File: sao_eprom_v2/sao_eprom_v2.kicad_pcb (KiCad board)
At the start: 4 copper layers, 65.1 x 55.1 mm, 75 parts, among them J1 Conn_01x03, J2 USB_C_Receptacle_USB2.0, J3 sao_v2_addon_tht, Q1 RE1C002UNTCL, Q2 RE1C002ZPTL, Q3 RE1C002UNTCL, Q4 RE1C002ZPTL, Q5 RE1C002UNTCL, Q6 RE1C002ZPTL, U1 W25Q128JVS, U10 AP3012, U2 RP2040, U3 24LC00, U4 74LS573, U5 multi_eprom, U6 74LVC4245A-Q100, U7 74LS573, U8 SY8079AAC, U9 AP3012, X1 SX3M12.000M20F30TNN

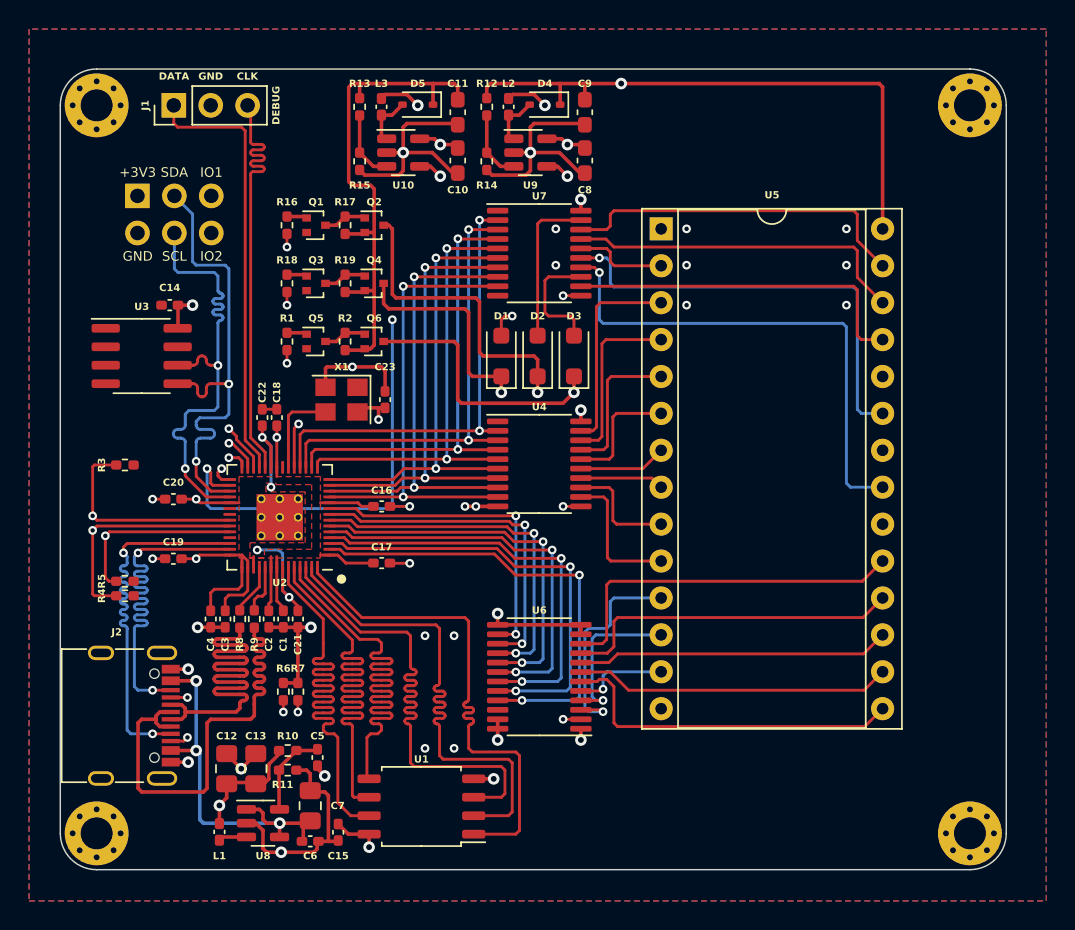
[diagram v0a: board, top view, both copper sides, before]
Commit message: Add some blinkenlights!
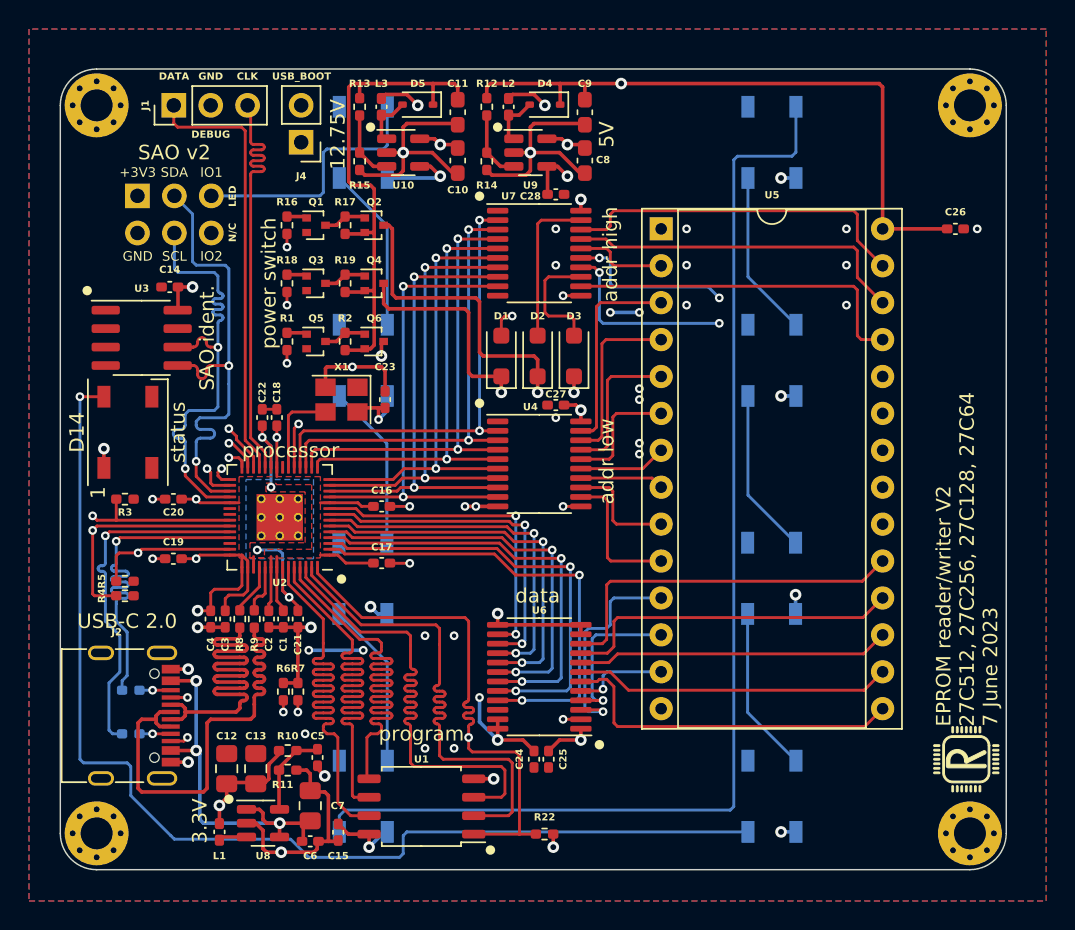
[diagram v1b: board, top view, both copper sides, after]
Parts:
- removed the REF** at (139.8, 61.0)
- added C24: 100n, Capacitor_SMD:C_0402_1005Metric_Pad0.74x0.62mm_HandSolder, F.Cu at (157.2, 77.8)
- added C25: 100n, Capacitor_SMD:C_0402_1005Metric_Pad0.74x0.62mm_HandSolder, F.Cu at (158.2, 77.8)
- added C26: 100n, Capacitor_SMD:C_0402_1005Metric_Pad0.74x0.62mm_HandSolder, F.Cu at (186.2, 41.2)
- added C27: 100n, Capacitor_SMD:C_0402_1005Metric_Pad0.74x0.62mm_HandSolder, F.Cu at (158.8, 53.4)
- added C28: 100n, Capacitor_SMD:C_0402_1005Metric_Pad0.74x0.62mm_HandSolder, F.Cu at (158.8, 38.9)
- added D10: WS2812B, LED_SMD:LED_WS2812B_PLCC4_5.0x5.0mm_P3.2mm, B.Cu at (173.6, 35.3)
- added D11: WS2812B, LED_SMD:LED_WS2812B_PLCC4_5.0x5.0mm_P3.2mm, B.Cu at (173.6, 50.3)
- added D12: WS2812B, LED_SMD:LED_WS2812B_PLCC4_5.0x5.0mm_P3.2mm, B.Cu at (173.6, 65.3)
- added D13: WS2812B, LED_SMD:LED_WS2812B_PLCC4_5.0x5.0mm_P3.2mm, B.Cu at (173.6, 80.3)
- added D14: WS2812B, LED_SMD:LED_WS2812B_PLCC4_5.0x5.0mm_P3.2mm, F.Cu at (129.3, 55.2)
- added D6: WS2812B, LED_SMD:LED_WS2812B_PLCC4_5.0x5.0mm_P3.2mm, B.Cu at (145.5, 35.3)
- added D7: WS2812B, LED_SMD:LED_WS2812B_PLCC4_5.0x5.0mm_P3.2mm, B.Cu at (145.5, 50.3)
- added D8: WS2812B, LED_SMD:LED_WS2812B_PLCC4_5.0x5.0mm_P3.2mm, B.Cu at (145.5, 65.3)
- added D9: WS2812B, LED_SMD:LED_WS2812B_PLCC4_5.0x5.0mm_P3.2mm, B.Cu at (145.5, 80.3)
- added J4: Conn_01x02, Connector_PinHeader_2.54mm:PinHeader_1x02_P2.54mm_Vertical, F.Cu at (141.2, 35.3)
- added R20: 27R, Resistor_SMD:R_0402_1005Metric_Pad0.72x0.64mm_HandSolder, B.Cu at (129.5, 76.0)
- added R21: 27R, Resistor_SMD:R_0402_1005Metric_Pad0.72x0.64mm_HandSolder, B.Cu at (129.5, 73.0)
- added R22: 1K, Resistor_SMD:R_0402_1005Metric_Pad0.72x0.64mm_HandSolder, F.Cu at (158.0, 82.9)
- added REF**: RobotMan2412_5mm, RobotMan2412:RobotMan2412_5mm, F.Cu at (187.0, 77.8)
- added REF**: RobotMan2412_10mm, RobotMan2412:RobotMan2412_10mm, B.Cu at (157.2, 57.8)
- moved R3 2.35 mm to (129.1, 59.9)
- moved C14 1.25 mm to (132.2, 45.2)
- moved U3 1.25 mm to (130.2, 48.8)
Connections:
- J3 pad 5: unconnected-(J3-IO1-Pad5) -> LED_DIN
- U2 pad 38: /Power generation/VdetEN -> Net-(U2-GPIO26_ADC0)
- U2 pad 39: unconnected-(U2-GPIO27_ADC1-Pad39) -> Net-(U2-GPIO27_ADC1)
- U2 pad 40: SBU1 -> unconnected-(U2-GPIO28_ADC2-Pad40)
- U2 pad 41: SBU2 -> /Power generation/VdetEN
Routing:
- net Net-(D10-DIN): track 0.00 -> 80.6 mm
- net Net-(D13-DOUT): track 0.00 -> 78.0 mm, vias 0 -> 1
- net /~{QSPI_CS}: track 34.9 -> 107.4 mm, vias 0 -> 1
- net +3V3: track 77.4 -> 118.5 mm, vias 18 -> 35
- net SBU2: track 26.7 -> 2.15 mm, vias 2 -> 1
- net SBU1: track 26.7 -> 2.15 mm, vias 2 -> 1
- net Net-(U2-GPIO26_ADC0): track 0.00 -> 24.4 mm, vias 0 -> 1
- net Net-(U2-GPIO27_ADC1): track 0.00 -> 24.4 mm, vias 0 -> 1
- net LED_DIN: track 0.00 -> 17.8 mm
- net Net-(D12-DOUT): track 0.00 -> 11.5 mm
- net Net-(D8-DOUT): track 0.00 -> 11.5 mm
- net Net-(D6-DOUT): track 0.00 -> 11.5 mm
- net Net-(D10-DOUT): track 0.00 -> 11.5 mm
- net Net-(D7-DOUT): track 0.00 -> 11.5 mm
- net Net-(D11-DOUT): track 0.00 -> 11.5 mm
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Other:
- board text added: "EPROM reader/writer V2 27C512, 27C256, 27C128, 27C64 7 June 2023"
- board text added: "LED"
- board text added: "N/C"
- board text added: "SAO ident."
- board text added: "SAO v2"
- board text added: "USB-C 2.0"
- board text added: "USB_BOOT"
- board text added: "addr high"
- board text added: "addr low"
- board text added: "data"
- board text added: "power switch"
- board text added: "processor"
- board text added: "program"
- board text added: "status"
- board text removed: "Address high"
- board text removed: "Address low"
- board text removed: "EPROM"
- board text removed: "Identification"
- board text removed: "Level shifter"
- board text removed: "Power switches"
- board text removed: "Program"

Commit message: Change LED order so status (on top) is first.
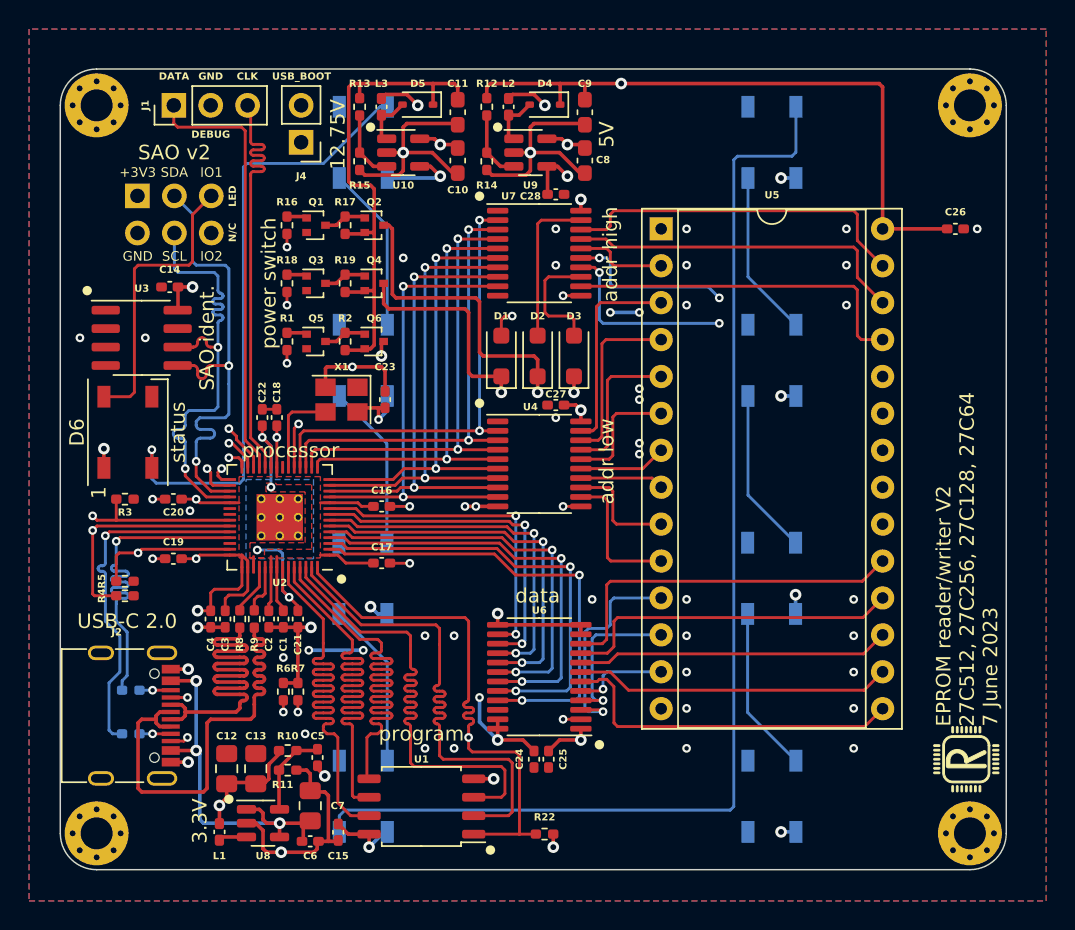
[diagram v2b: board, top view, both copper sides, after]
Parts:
- D14: moved to B.Cu
- D6: moved to F.Cu
- moved D10 53.1 mm to (145.5, 80.3)
- moved D14 50.9 mm to (173.6, 80.3)
- moved D6 25.7 mm to (129.3, 55.2)
- moved D12 15.0 mm to (173.6, 50.3)
- moved D13 15.0 mm to (173.6, 65.3)
- moved D8 15.0 mm to (145.5, 50.3)
- moved D9 15.0 mm to (145.5, 65.3)
- moved D11 15.0 mm to (173.6, 35.3)
- moved D7 15.0 mm to (145.5, 35.3)
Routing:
- net Net-(D10-DOUT): track 11.5 -> 80.6 mm
- net Net-(D10-DIN): track 80.6 -> 11.5 mm
- net Net-(D13-DOUT): track 78.0 -> 11.5 mm, vias 1 -> 0
- net Net-(D6-DOUT): track 11.5 -> 42.9 mm, vias 0 -> 1
- net LED_DIN: track 17.8 -> 20.0 mm
- net GND: vias 32 -> 48

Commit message: Now with QWIIC and TestPads!
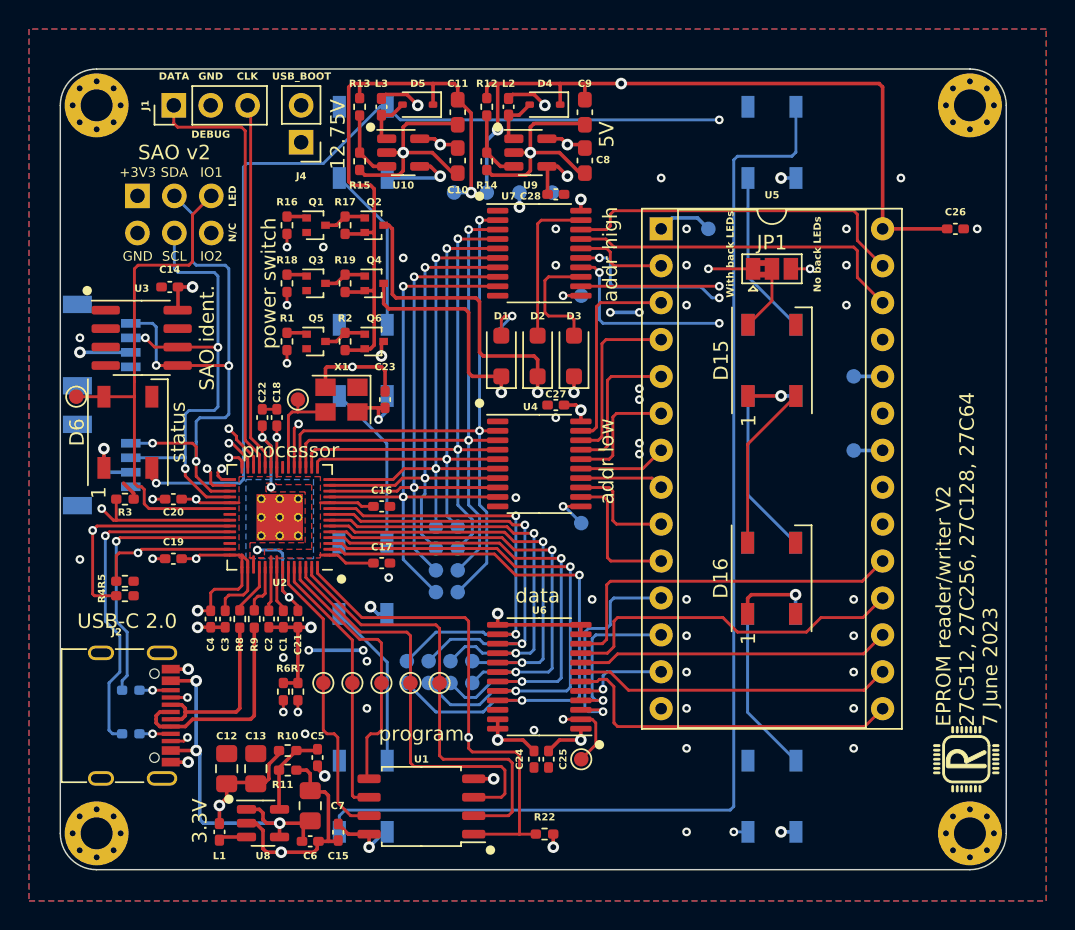
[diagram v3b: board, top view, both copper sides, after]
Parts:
- added D15: WS2812B, LED_SMD:LED_WS2812B_PLCC4_5.0x5.0mm_P3.2mm, F.Cu at (173.6, 50.3)
- added D16: WS2812B, LED_SMD:LED_WS2812B_PLCC4_5.0x5.0mm_P3.2mm, F.Cu at (173.6, 65.3)
- added J5: I2C, qwiic:1X04_1MM_RA_GND, B.Cu at (129.5, 49.2)
- added J6: I2C, qwiic:1X04_1MM_RA_GND, B.Cu at (129.5, 57.5)
- added JP1: SolderJumper, Jumper:SolderJumper-3_P1.3mm_Bridged2Bar12_Pad1.0x1.5mm, F.Cu at (173.6, 44.0)
- added TP1: TestPoint, TestPoint:TestPoint_Pad_D1.0mm, F.Cu at (125.8, 52.8)
- added TP10: TestPoint, TestPoint:TestPoint_Pad_D1.0mm, B.Cu at (152.0, 61.8)
- added TP11: TestPoint, TestPoint:TestPoint_Pad_D1.0mm, B.Cu at (152.0, 63.2)
- added TP12: TestPoint, TestPoint:TestPoint_Pad_D1.0mm, B.Cu at (152.0, 64.8)
- added TP13: TestPoint, TestPoint:TestPoint_Pad_D1.0mm, B.Cu at (152.0, 66.2)
- added TP14: TestPoint, TestPoint:TestPoint_Pad_D1.0mm, B.Cu at (148.5, 72.5)
- added TP15: TestPoint, TestPoint:TestPoint_Pad_D1.0mm, B.Cu at (150.0, 72.5)
- added TP16: TestPoint, TestPoint:TestPoint_Pad_D1.0mm, B.Cu at (151.5, 72.5)
- added TP17: TestPoint, TestPoint:TestPoint_Pad_D1.0mm, B.Cu at (153.0, 72.5)
- added TP18: TestPoint, TestPoint:TestPoint_Pad_D1.0mm, B.Cu at (153.0, 71.0)
- added TP19: TestPoint, TestPoint:TestPoint_Pad_D1.0mm, B.Cu at (151.5, 71.0)
- added TP2: TestPoint, TestPoint:TestPoint_Pad_D1.0mm, F.Cu at (160.5, 77.8)
- added TP20: TestPoint, TestPoint:TestPoint_Pad_D1.0mm, B.Cu at (150.0, 71.0)
- added TP21: TestPoint, TestPoint:TestPoint_Pad_D1.0mm, B.Cu at (148.5, 71.0)
- added TP22: TestPoint, TestPoint:TestPoint_Pad_D1.0mm, B.Cu at (156.2, 38.8)
- added TP23: TestPoint, TestPoint:TestPoint_Pad_D1.0mm, B.Cu at (154.0, 38.8)
- added TP24: TestPoint, TestPoint:TestPoint_Pad_D1.0mm, B.Cu at (151.8, 38.8)
- added TP25: TestPoint, TestPoint:TestPoint_Pad_D1.0mm, B.Cu at (179.2, 51.4)
- added TP26: TestPoint, TestPoint:TestPoint_Pad_D1.0mm, B.Cu at (169.2, 41.2)
- added TP27: TestPoint, TestPoint:TestPoint_Pad_D1.0mm, B.Cu at (179.2, 56.5)
- added TP28: TestPoint, TestPoint:TestPoint_Pad_D1.0mm, F.Cu at (141.0, 53.0)
- added TP29: TestPoint_Small, TestPoint:TestPoint_Pad_D1.0mm, F.Cu at (144.8, 72.5)
- added TP3: TestPoint, TestPoint:TestPoint_Pad_D1.0mm, B.Cu at (155.0, 48.5)
- added TP30: TestPoint_Small, TestPoint:TestPoint_Pad_D1.0mm, F.Cu at (146.8, 72.5)
- added TP31: TestPoint_Small, TestPoint:TestPoint_Pad_D1.0mm, F.Cu at (150.8, 72.5)
- added TP32: TestPoint_Small, TestPoint:TestPoint_Pad_D1.0mm, F.Cu at (148.8, 72.5)
- added TP33: TestPoint_Small, TestPoint:TestPoint_Pad_D1.0mm, F.Cu at (142.8, 72.5)
- added TP34: TestPoint, TestPoint:TestPoint_Pad_D1.0mm, B.Cu at (158.5, 38.8)
- added TP4: TestPoint, TestPoint:TestPoint_Pad_D1.0mm, B.Cu at (160.5, 61.5)
- added TP5: TestPoint, TestPoint:TestPoint_Pad_D1.0mm, B.Cu at (160.5, 45.9)
- added TP6: TestPoint, TestPoint:TestPoint_Pad_D1.0mm, B.Cu at (150.5, 66.2)
- added TP7: TestPoint, TestPoint:TestPoint_Pad_D1.0mm, B.Cu at (150.5, 64.8)
- added TP8: TestPoint, TestPoint:TestPoint_Pad_D1.0mm, B.Cu at (150.5, 63.2)
- added TP9: TestPoint, TestPoint:TestPoint_Pad_D1.0mm, B.Cu at (150.5, 61.8)
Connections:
- D14 pad 2: /Blinkenlights/Dout -> Net-(D14-DOUT)
- U2 pad 34: unconnected-(U2-GPIO22-Pad34) -> LED_DIN
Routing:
- net Net-(D14-DOUT): track 0.00 -> 43.5 mm, vias 0 -> 2
- net Net-(D6-DOUT): track 42.9 -> 81.3 mm, vias 1 -> 3
- net USB_D-: track 32.5 -> 12.1 mm
- net USB_D+: track 32.5 -> 14.8 mm
- net /QSPI_D0: track 34.8 -> 18.4 mm
- net /QSPI_CLK: track 34.8 -> 18.6 mm
- net LED_DIN: track 20.0 -> 35.9 mm
- net /QSPI_D3: track 34.8 -> 20.4 mm
- net /EPROM and level shifters/A7: track 31.7 -> 43.9 mm
- net Net-(D15-DOUT): track 0.00 -> 11.5 mm
- net +3V3: track 118.5 -> 129.6 mm, vias 35 -> 36
- net /EPROM and level shifters/A6: track 31.4 -> 41.3 mm
- net /EPROM and level shifters/D0: track 32.0 -> 41.1 mm
- net /EPROM and level shifters/D7: track 22.4 -> 30.8 mm
- net SDA: track 33.5 -> 41.8 mm, vias 2 -> 4
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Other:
- board text added: "No back LEDs"
- board text added: "QWIIC"
- board text added: "With back LEDs"
- board text removed: "Length tuned"

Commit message: Label the test pads
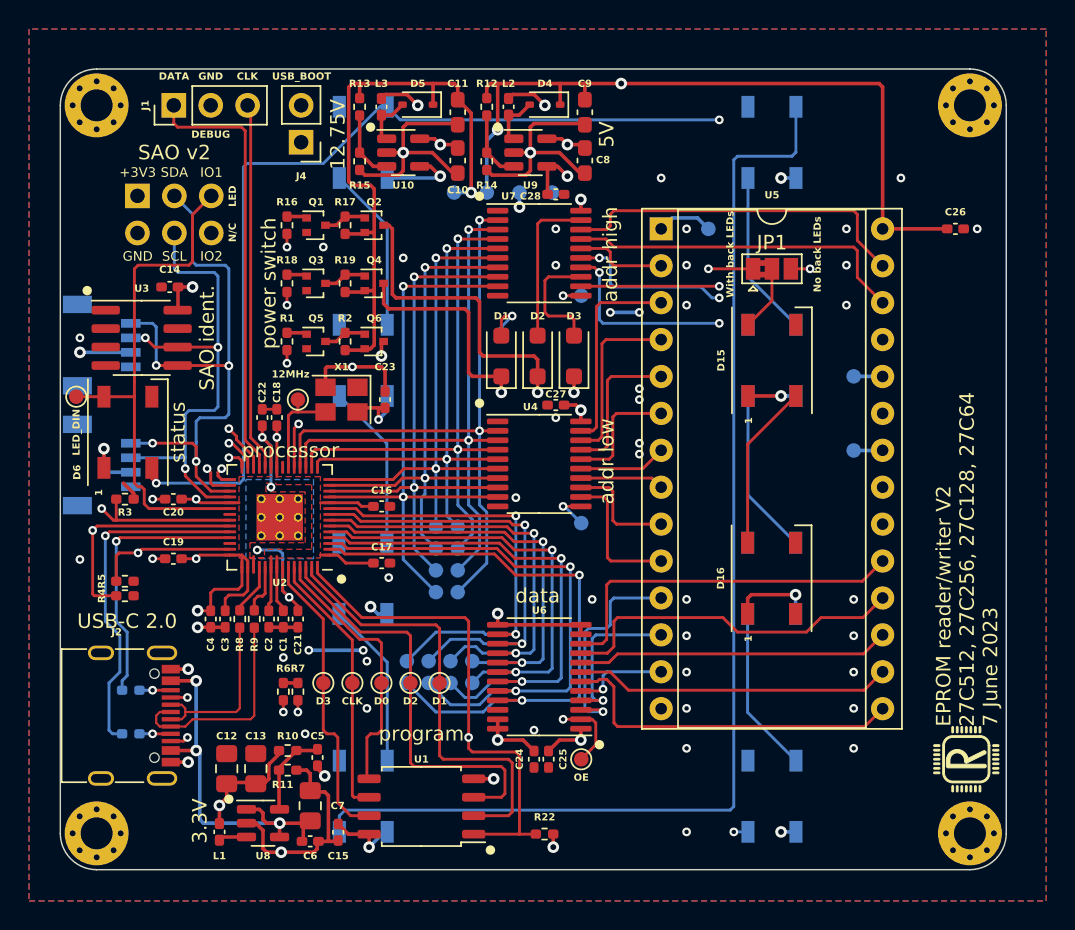
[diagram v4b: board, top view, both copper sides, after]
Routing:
- net GND: track 81.4 -> 76.7 mm, vias 48 -> 47
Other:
- board text added: "0"
- board text added: "1"
- board text added: "12MHz"
- board text added: "12V75"
- board text added: "2"
- board text added: "3"
- board text added: "3v3"
- board text added: "4"
- board text added: "5"
- board text added: "6"
- board text added: "7"
- board text added: "AHS"
- board text added: "ALS"
- board text added: "D0"
- board text added: "D1"
- board text added: "D2"
- board text added: "D3"
- board text added: "LED_DIN"
- board text added: "OE"
- board text added: "Vdet"
- board text added: "VppA"
- board text added: "VppB"
- board text added: "addr"
- board text added: "~{OE}"

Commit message: Bump date
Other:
- board text added: "EPROM reader/writer V2 27C512, 27C256, 27C128, 27C64 8 June 2023"
- board text removed: "EPROM reader/writer V2 27C512, 27C256, 27C128, 27C64 7 June 2023"
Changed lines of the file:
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@@
     (effects (font (size 0.66 0.66) (thickness 0.1)) (justify bottom))
   )
-  (gr_text "EPROM reader/writer V2\n27C512, 27C256, 27C128, 27C64\n7 June 2023" (at 189.25 75.5 90) (layer "F.SilkS")
+  (gr_text "EPROM reader/writer V2\n27C512, 27C256, 27C128, 27C64\n8 June 2023" (at 189.25 75.5 90) (layer "F.SilkS")
     (effects (font (size 1 1) (thickness 0.15)) (justify left bottom))
   )

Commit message: Most important commit in the history of the entire world
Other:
- board text added: "3V3"
- board text removed: "3v3"
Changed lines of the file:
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@@
     (effects (font (size 0.5 0.5) (thickness 0.1) bold) (justify mirror))
   )
-  (gr_text "3v3" (at 156.25 36.75) (layer "B.SilkS")
+  (gr_text "3V3" (at 156.25 36.75) (layer "B.SilkS")
     (effects (font (size 0.5 0.5) (thickness 0.1) bold) (justify mirror))
   )
